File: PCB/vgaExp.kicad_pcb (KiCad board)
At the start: 2 copper layers, 80 x 60.1 mm, 78 parts, among them J1 DE-15, J2 DE-15, J3 VHDCI, P5 CONN_1, P6 CONN_1, P7 CONN_6, U1 ADP3303-3V3, U2 ADP3334, U3 AD9984, U4 ADP3334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

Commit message: Changing Layout
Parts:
- moved Cp4 98.1 mm to (227.3, 62.3)
- moved Cp6 98.1 mm to (245.7, 62.0)
- moved R17 98.1 mm to (237.3, 58.0)
- moved U6 98.1 mm to (240.5, 66.7)
- moved Cp1 98.1 mm to (199.2, 61.9)
- moved Cp5 98.1 mm to (216.1, 62.0)
- moved R10 98.1 mm to (221.7, 64.8)
- moved TP13 98.1 mm to (194.5, 67.0)
- moved TP9 98.1 mm to (214.2, 65.0)
- moved U1 98.1 mm to (206.7, 61.9)
- moved C2 98.1 mm to (205.5, 65.9)
- moved C24 98.1 mm to (237.7, 68.1)
- moved C25 98.1 mm to (237.7, 69.9)
- moved C3 98.1 mm to (205.5, 67.9)
- moved C4 98.1 mm to (205.5, 70.1)
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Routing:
- net /I2C/DDC Section/OVDD: track 215.2 -> 0.00 mm, vias 8 -> 0
- net /I2C/DDC Section/VCC: track 188.5 -> 0.00 mm, vias 2 -> 0
- net /I2C/DDC Section/GND: track 144.2 -> 0.00 mm, vias 19 -> 0
- net /HSYNC0: track 131.4 -> 0.00 mm, vias 1 -> 0
- net /VSYNC0: track 128.3 -> 0.00 mm
- net /PowerSupply/VD: track 100.5 -> 0.00 mm, vias 5 -> 0
- net /I2C/DDC Section/SDA_VGA_RX_BUF: track 65.9 -> 0.00 mm
- net /I2C/DDC Section/SCL_VGA_RX_BUF: track 63.7 -> 0.00 mm
- net /VSOUT: track 59.3 -> 0.00 mm, vias 1 -> 0
- net /I2C/DDC Section/SDA_VGA_TX_BUF: track 58.9 -> 0.00 mm, vias 3 -> 0
- net /HSOUT: track 51.2 -> 0.00 mm, vias 1 -> 0
- net /I2C/DDC Section/SCL_VGA_TX_BUF: track 50.8 -> 0.00 mm, vias 1 -> 0
- net /PowerSupply/PVD: track 49.4 -> 0.00 mm, vias 1 -> 0
- net /SOGOUT: track 48.0 -> 0.00 mm, vias 1 -> 0
- net /DATACK: track 47.5 -> 0.00 mm, vias 1 -> 0
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- removed copper zone on B.Cu, net /I2C/DDC Section/GND
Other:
- board size 80 x 60.1 mm -> 80 x 91.1 mm

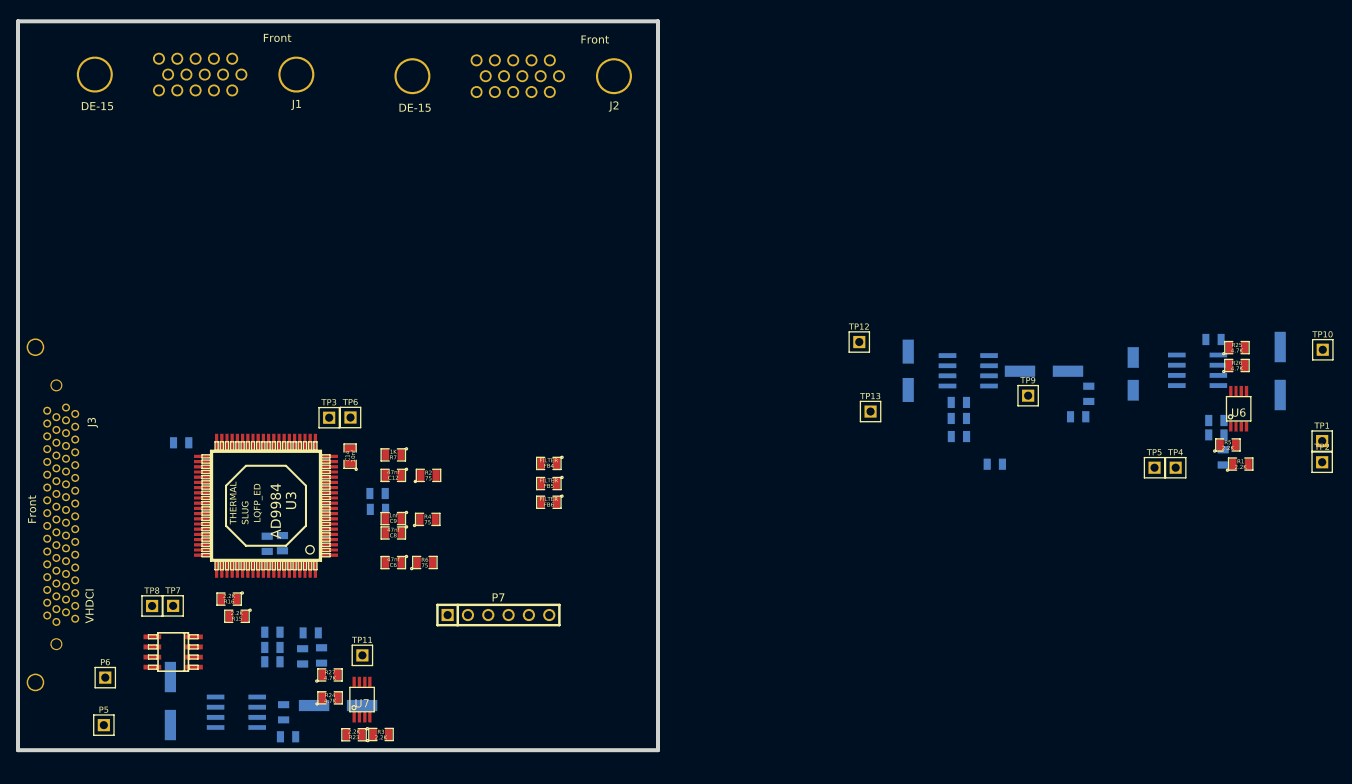
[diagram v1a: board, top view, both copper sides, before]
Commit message: Layout changes and initial rough placement
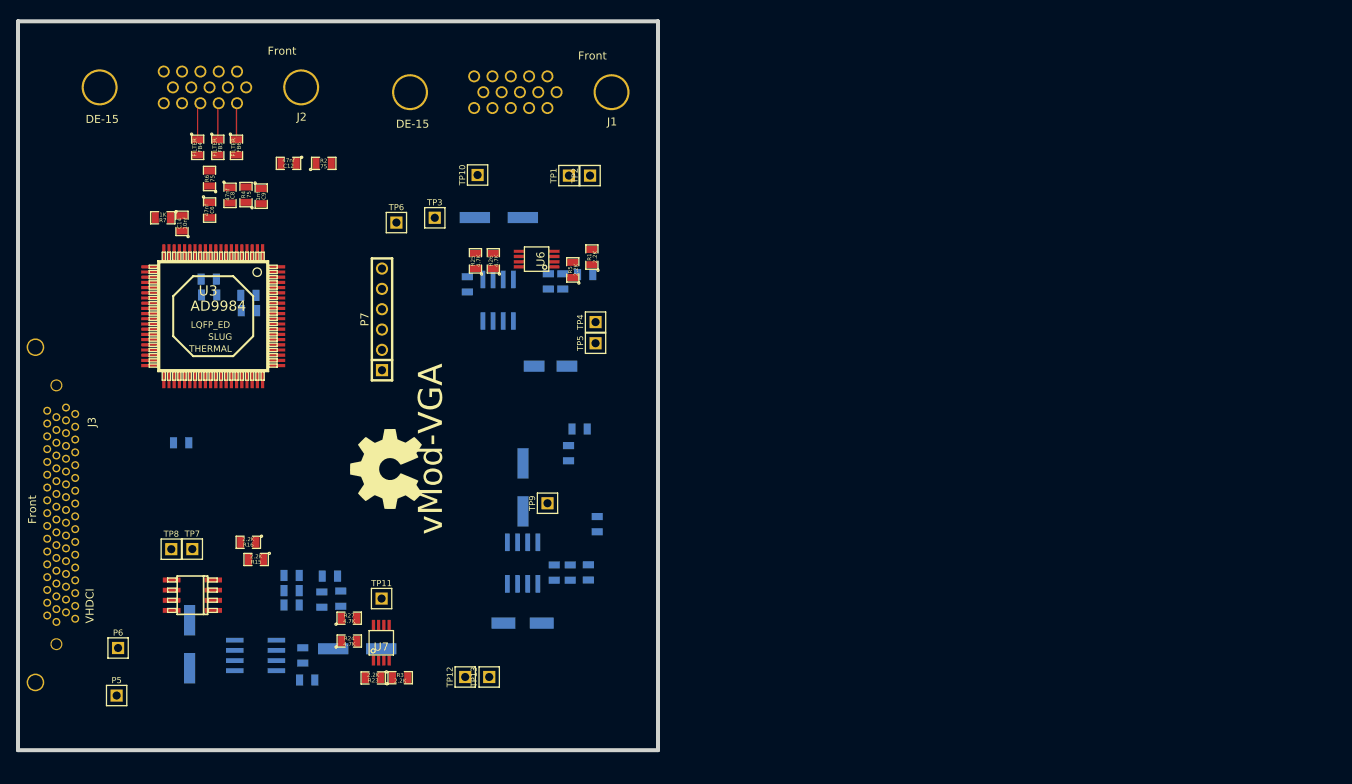
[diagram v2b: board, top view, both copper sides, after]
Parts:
- ?: moved to F.Cu
- moved TP10 107.9 mm to (145.3, 37.5), turned to 90 degrees
- moved TP1 99.8 mm to (156.8, 37.5), turned to 90 degrees
- moved Cp6 99.5 mm to (148.0, 42.8), turned to 180 degrees
- moved TP2 98.3 mm to (159.4, 37.5), turned to 90 degrees
- moved R25 95.8 mm to (145.1, 48.2), turned to 90 degrees
- moved R26 93.9 mm to (147.3, 48.2), turned to 90 degrees
- moved R17 93.5 mm to (144.1, 51.1), turned to 90 degrees
- moved U6 89.7 mm to (152.7, 48.0), turned to 90 degrees
- moved U4 87.9 mm to (147.9, 53.1), turned to 180 degrees
- moved C24 85.3 mm to (154.2, 50.8), turned to 90 degrees
- moved R1 85.1 mm to (159.6, 47.7), turned to 90 degrees
- moved R5 84.8 mm to (157.2, 49.3), turned to 90 degrees
- moved C25 83.9 mm to (156.0, 50.8), turned to 90 degrees
- moved R18 83.0 mm to (158.8, 49.9), turned to 180 degrees
- moved TP4 74.8 mm to (160.1, 55.8), turned to 90 degrees
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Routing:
- net /B: track 0.00 -> 4.71 mm
- net /G: track 0.00 -> 4.61 mm
- net /R: track 0.00 -> 4.59 mm

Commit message: routing 30% complete
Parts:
- removed ?: , OSHW-logo_silkscreen-back_10mm
- added l1: e, OSHW-logo_silkscreen-back_10mm, F.Cu at (132.2, 76.1)
- moved U7 60.7 mm to (136.5, 35.3)
- moved C21 39.9 mm to (146.6, 59.7)
- moved R15 28.5 mm to (129.1, 59.4), turned to 270 degrees
- moved R16 25.1 mm to (127.0, 60.4), turned to 270 degrees
- moved TP8 19.3 mm to (122.4, 95.9), turned to 180 degrees
- moved R2 16.5 mm to (110.0, 39.7), turned to 180 degrees
- moved TP7 15.5 mm to (119.8, 95.9), turned to 180 degrees
- moved C12 11.2 mm to (113.2, 43.3), turned to 270 degrees
- moved U5 9.36 mm to (110.5, 99.3)
- moved C6 9.29 mm to (121.0, 43.3)
- moved R6 7.37 mm to (119.0, 39.6), turned to 180 degrees
- moved R7 5.30 mm to (111.3, 43.3), turned to 270 degrees
- moved C8 5.20 mm to (118.4, 43.3)
- moved P7 4.82 mm to (138.2, 55.9), turned to 270 degrees
- moved J1 3.75 mm to (145.8, 24.5)
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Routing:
- net /B0: track 0.00 -> 57.4 mm
- net /B1: track 0.00 -> 56.4 mm
- net /B2: track 0.00 -> 55.2 mm, vias 0 -> 1
- net /B3: track 0.00 -> 50.0 mm, vias 0 -> 1
- net /B6: track 0.00 -> 47.6 mm, vias 0 -> 1
- net /B4: track 0.00 -> 47.5 mm
- net /B5: track 0.00 -> 45.1 mm
- net /B7: track 0.00 -> 45.1 mm
- net /G0: track 0.00 -> 41.5 mm, vias 0 -> 1
- net /B8: track 0.00 -> 40.8 mm
- net /B9: track 0.00 -> 40.3 mm
- net /G1: track 0.00 -> 38.7 mm, vias 0 -> 1
- net /G2: track 0.00 -> 35.5 mm
- net /R0: track 0.00 -> 33.2 mm
- net /G3: track 0.00 -> 33.2 mm
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
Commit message: Added Standoffs. Fixed Issue #11
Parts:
- added -: -, STAND-OFF, F.Cu at (91.9, 22.3)
- added -: -, STAND-OFF, F.Cu at (164.1, 22.3)
- added -: -, STAND-OFF, F.Cu at (92.0, 105.8)
- added -: -, STAND-OFF, F.Cu at (164.2, 105.7)
- moved R1 65.8 mm to (93.8, 48.4), turned to 0 degrees
- moved R5 63.4 mm to (93.9, 46.3), turned to 0 degrees
- moved U6 59.5 mm to (93.6, 41.5), turned to 0 degrees
- moved R26 55.3 mm to (93.3, 36.0), turned to 0 degrees
- moved R25 53.7 mm to (93.3, 33.8), turned to 0 degrees
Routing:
- net /G4: track 0.00 -> 34.7 mm

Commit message: Fixed #11
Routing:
- net /DATACK: track 17.5 -> 12.9 mm
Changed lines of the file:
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@@
     (thickness 1.6)
     (drawings 7)
-    (tracks 296)
+    (tracks 295)
     (zones 0)
     (modules 82)
@@
   (segment (start 117.7733 77.0267) (end 109.08 85.72) (width 0.125) (layer F.Cu) (net 11))
   (segment (start 107.5 52.62622) (end 105.71378 52.62622) (width 0.125) (layer F.Cu) (net 14))
-  (segment (start 97.82 60.52) (end 97.82 65.07) (width 0.125) (layer F.Cu) (net 14))
   (segment (start 105.71378 52.62622) (end 97.82 60.52) (width 0.125) (layer F.Cu) (net 14))
   (segment (start 112.8722 33.0433) (end 112.8722 28.5978) (width 0.125) (layer F.Cu) (net 15))

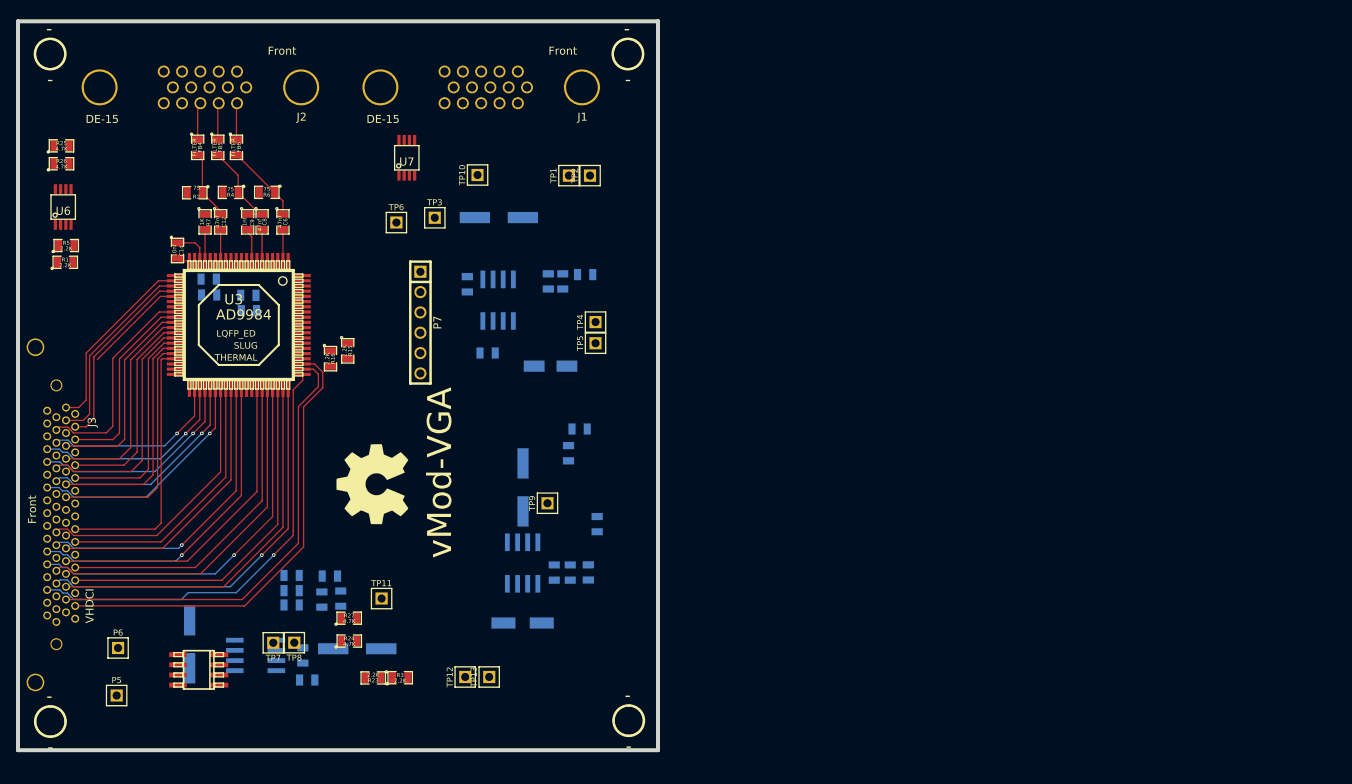
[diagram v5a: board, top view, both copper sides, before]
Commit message: Added GND Testpoint. Fixes #10
Added GND Testpoint at board's periphery
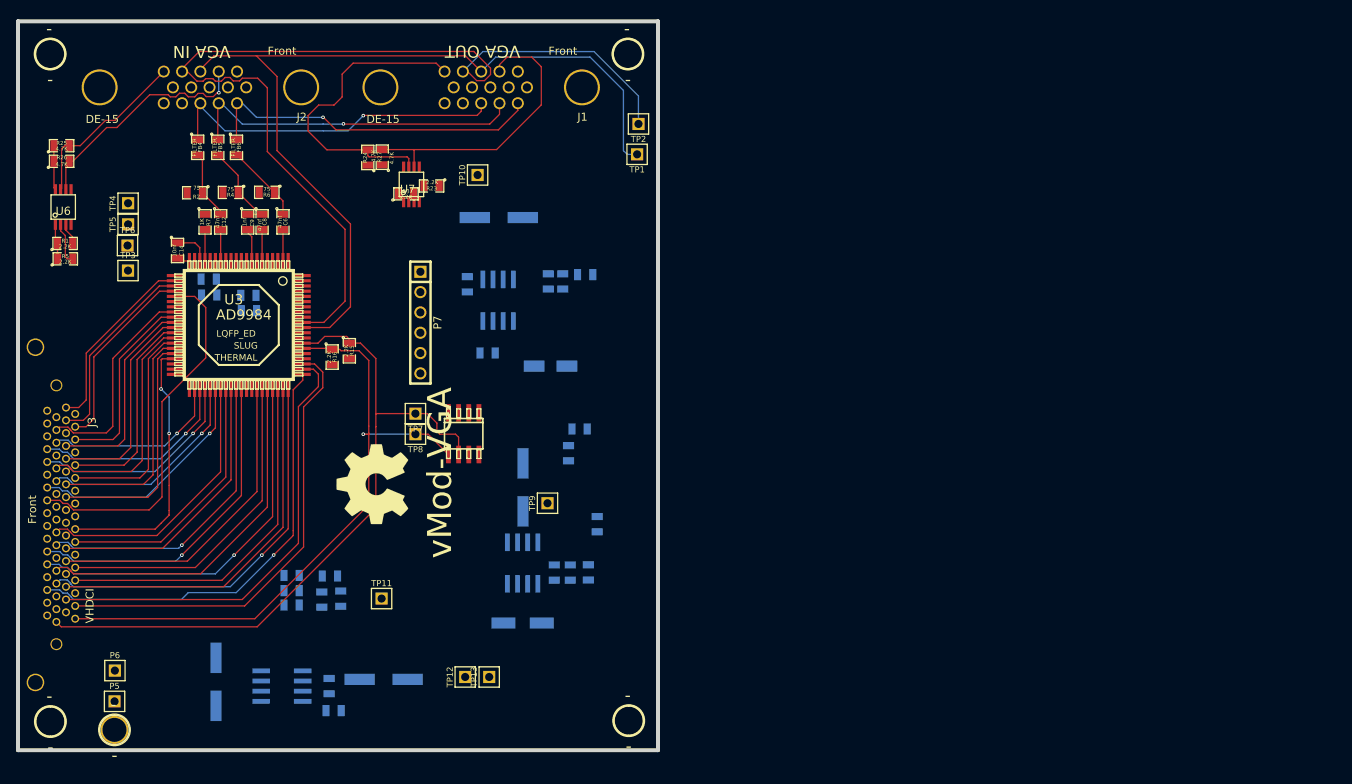
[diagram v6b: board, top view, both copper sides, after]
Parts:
- added -: -, GND-HOLE, F.Cu at (100.0, 106.8)
- moved R23 61.9 mm to (139.6, 38.8)
- moved R24 60.5 mm to (131.6, 35.3), turned to 90 degrees
- moved R3 60.5 mm to (136.4, 39.8)
- moved TP4 60.3 mm to (101.7, 41.0)
- moved TP5 60.3 mm to (101.7, 43.6)
- moved R27 57.8 mm to (133.4, 35.2), turned to 90 degrees
- moved U5 44.4 mm to (143.6, 69.8), turned to 180 degrees
- moved TP3 38.9 mm to (101.7, 49.4)
- moved TP6 33.7 mm to (101.6, 46.3)
- moved TP7 33.7 mm to (137.6, 67.3)
- moved TP8 30.1 mm to (137.6, 69.8)
- moved TP1 8.93 mm to (165.3, 34.9), turned to 180 degrees
- moved TP2 8.85 mm to (165.5, 31.1), turned to 180 degrees
- moved Cp2 5.74 mm to (112.6, 100.8)
- moved R13 5.05 mm to (126.8, 101.3)
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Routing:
- net /VSYNC0: track 0.00 -> 124.0 mm
- net /HSYNC0: track 0.00 -> 109.8 mm
- net /I2C/DDC Section/SCL_INT: track 0.00 -> 90.3 mm
- net /I2C/DDC Section/SDA_INT: track 0.00 -> 81.9 mm, vias 0 -> 1
- net /I2C/DDC Section/SCL_VGA_TX: track 0.00 -> 39.3 mm
- net /B: track 4.71 -> 43.5 mm, vias 0 -> 1
- net /R: track 4.59 -> 43.1 mm, vias 0 -> 1
- net /G: track 4.61 -> 42.7 mm, vias 0 -> 1
- net /I2C/DDC Section/SDA_VGA_TX: track 0.00 -> 36.1 mm
- net /DATACK: track 12.9 -> 46.0 mm
- net /I2C/DDC Section/SDA_VGA_RX: track 0.00 -> 29.5 mm, vias 0 -> 1
- net /I2C/DDC Section/SCL_VGA_RX: track 0.00 -> 22.2 mm
- net /I2C/DDC Section/VCC: track 0.00 -> 5.52 mm
- net /I2C/DDC Section/SCL_VGA_RX_BUF: track 0.00 -> 5.29 mm
- net /I2C/DDC Section/OVDD: track 0.00 -> 4.37 mm
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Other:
- board text added: "VGA IN"
- board text added: "VGA OUT"

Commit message: Progress so far
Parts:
- moved C5 59.4 mm to (107.6, 53.7), turned to 180 degrees
- moved Cp2 58.8 mm to (161.2, 67.7), turned to 180 degrees
- moved C2 53.6 mm to (107.8, 61.8), turned to 270 degrees
- moved R14 50.2 mm to (153.1, 61.3), turned to 180 degrees
- moved C25 49.3 mm to (108.8, 65.1)
- moved U2 46.9 mm to (151.4, 65.8), turned to 270 degrees
- moved R9 46.4 mm to (114.2, 53.7), turned to 0 degrees
- moved C3 46.2 mm to (116.8, 64.3), turned to 270 degrees
- moved R10 45.8 mm to (114.2, 55.9)
- moved C4 44.8 mm to (123.4, 60.2), turned to 180 degrees
- moved C16 42.9 mm to (126.6, 47.5)
- moved C15 42.9 mm to (124.7, 47.7)
- moved R8 42.8 mm to (125.6, 44.8)
- moved Cp3 42.1 mm to (142.0, 59.3), turned to 270 degrees
- moved R13 40.4 mm to (146.0, 65.8), turned to 90 degrees
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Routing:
- net /I2C/DDC Section/VCC: track 5.52 -> 159.8 mm
- net /I2C/DDC Section/GND: track 0.00 -> 67.0 mm, vias 0 -> 1
- net (no net): track 0.00 -> 17.3 mm
- net /PowerSupply/PVD: track 0.00 -> 14.9 mm
- net /PowerSupply/VD: track 0.00 -> 14.7 mm
- net N-0000086: track 0.00 -> 9.52 mm
- net /I2C/DDC Section/SCL_INT: track 90.3 -> 81.0 mm
- net N-0000085: track 0.00 -> 9.22 mm
- net /I2C/DDC Section/SDA_INT: track 81.9 -> 76.7 mm
- added copper zone on B.Cu, net /I2C/DDC Section/GND
